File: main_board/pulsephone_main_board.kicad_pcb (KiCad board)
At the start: 6 copper layers, 49.8 x 52.8 mm, 21 parts, among them J1 Conn_2Rows-59Pins, J2 Conn_2Rows-59Pins, J4 Conn_2Rows-59Pins, J5 Conn_2Rows-59Pins, U1 TPS62840DLCR, U2 PCM5102APWR

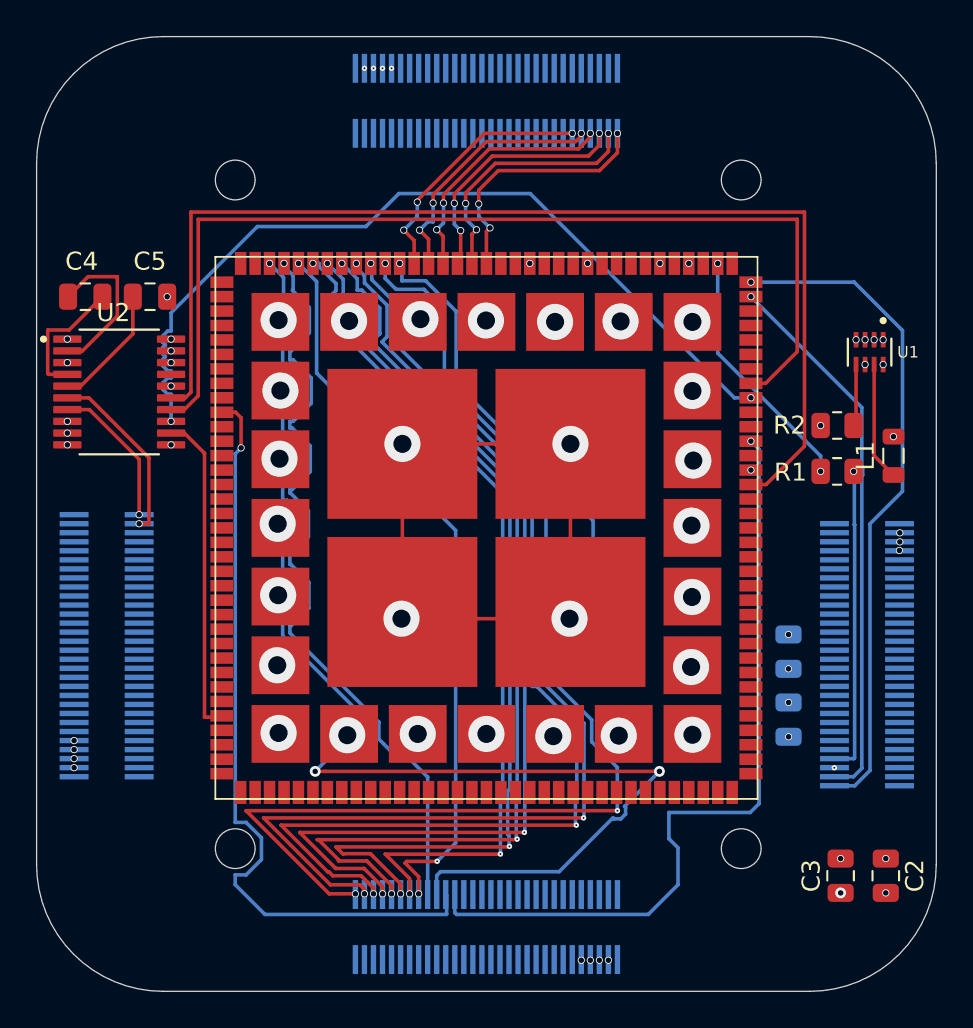
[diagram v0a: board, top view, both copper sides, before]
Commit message: replaced all power connections with copper pads and started drawing traces to them.
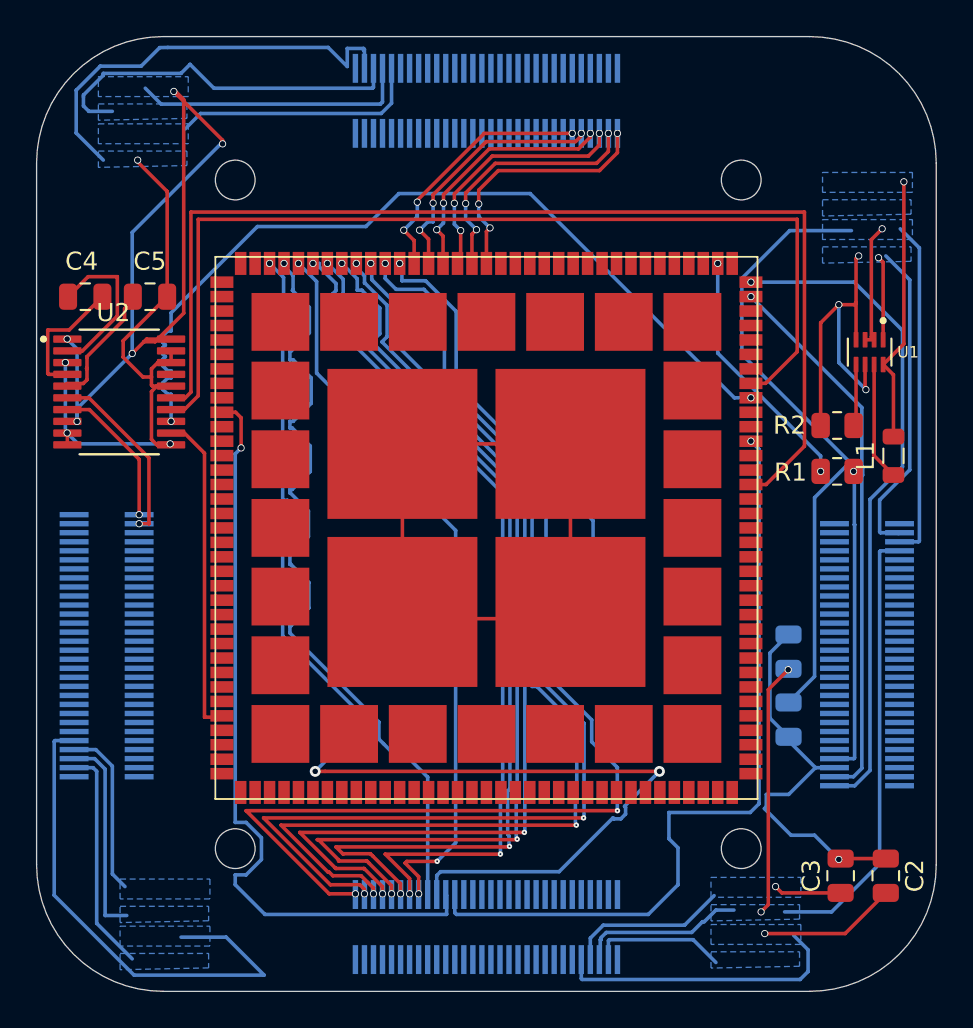
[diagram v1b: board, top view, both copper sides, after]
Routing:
- net GND: track 43.8 -> 185.7 mm, vias 50 -> 9
- net +5V: track 0.00 -> 126.6 mm, vias 12 -> 2
- net +3.3V: track 0.00 -> 97.9 mm, vias 9 -> 7
- net +3.7VBAT: track 0.00 -> 80.2 mm, vias 5 -> 2
- added copper zone on B.Cu, net +3.3V
- added copper zone on B.Cu, net +3.7VBAT
- added copper zone on B.Cu, net +5V
- added copper zone on B.Cu, net GND
- removed copper zone on In2.Cu, net +3.3V
- removed copper zone on In3.Cu, net +3.7VBAT
- removed copper zone on In1.Cu, net +5V
- removed copper zone on In4.Cu, net GND
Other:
- copper layers 6 -> 2

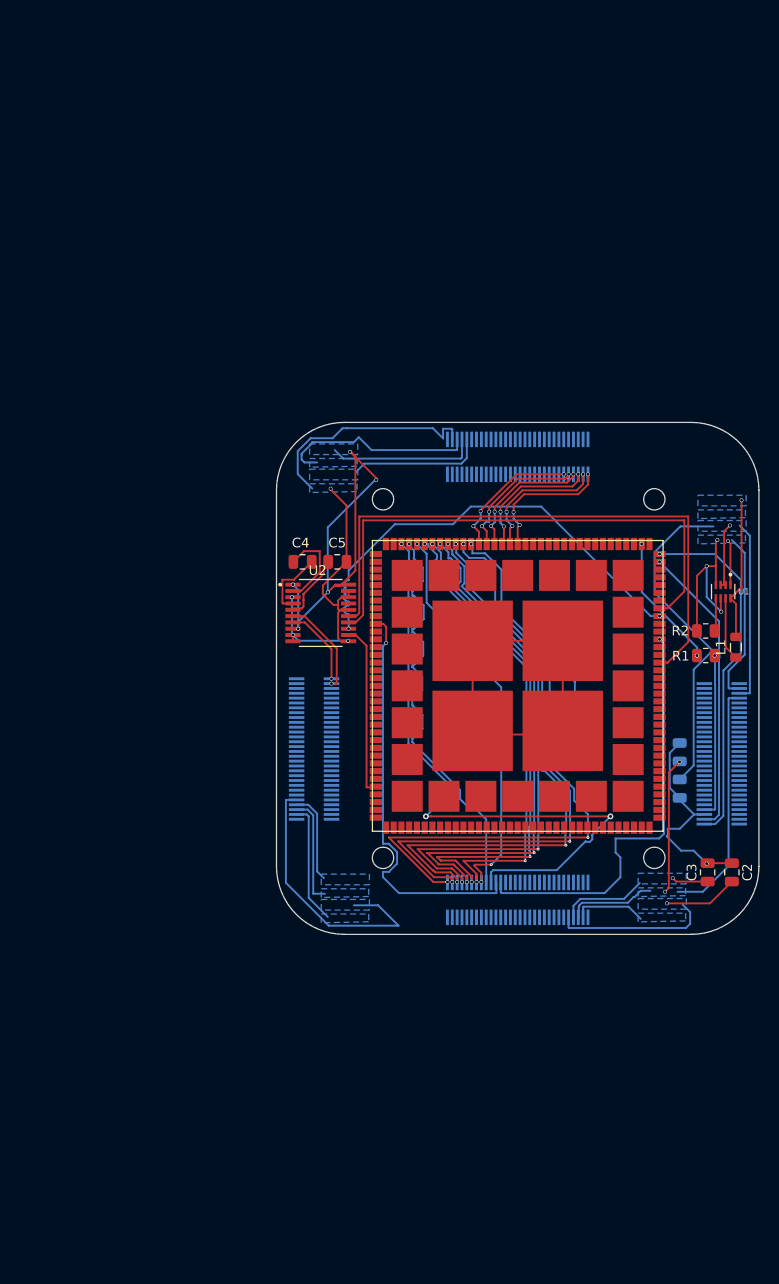
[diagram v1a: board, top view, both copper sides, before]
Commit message: Refactor the main board design
Mainboard is now one big pcb which is the shape and size of the phone. Modules will now attach on top of main board
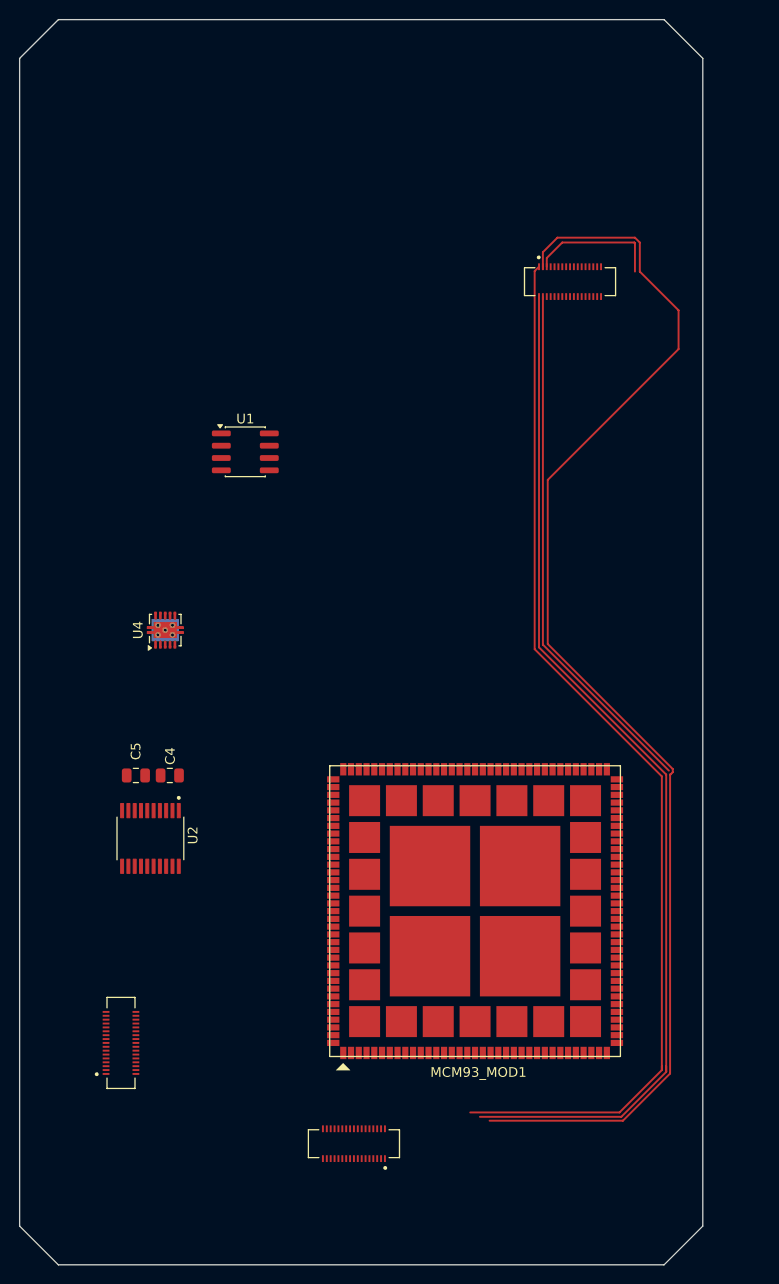
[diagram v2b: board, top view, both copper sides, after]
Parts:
- removed ? (x2): , 
- removed C1, C6: 22uF, Capacitor_SMD:C_0805_2012Metric
- removed C2: 4.7uF, Capacitor_SMD:C_0805_2012Metric
- removed C3: 10uF, Capacitor_SMD:C_0805_2012Metric
- removed G***: LOGO, LOGO
- removed J1, J2: Conn_2Rows-59Pins, Connector_Hirose:Hirose_DF12_DF12E3.0-60DP-0.5V_2x30_P0.50mm_Vertical
- removed L1: 2.2uH, Inductor_SMD:L_0805_2012Metric
- removed R1: 100Kohm, Resistor_SMD:R_0805_2012Metric
- removed R2: 267K, Resistor_SMD:R_0805_2012Metric
- removed REF** (x2): MountingHole_2.2mm_M2, MountingHole:MountingHole_2.2mm_M2
- added J3: Conn_2Rows-35Pins_MountingPin, DF40-34P:HIROSE_DF40C-34DS-0.4V_58_, F.Cu at (157.8, 53.0)
- added U4: TPS61202DRC, Package_SON:Texas_S-PVSON-N10_ThermalVias, F.Cu at (116.0, 89.0)
- J4, J5: value Conn_2Rows-59Pins -> Conn_2Rows-35Pins_MountingPin; footprint Connector_Hirose:Hirose_DF12_DF12E3.0-60DP-0.5V_2x30_P0.50mm_Vertical -> DF40-34P:HIROSE_DF40C-34DS-0.4V_58_; moved to F.Cu
- MCM93_MOD1: footprint LGA:LGA-140-080-30x30-iMX93 -> mcm-imx93_footprint:LGA-140-080-30x30-iMX93
- U1: value TPS62840DLCR -> XL1509-3.3; footprint TPS62840:SON50P200X150X100-8N -> Package_SO:SOIC-8_3.9x4.9mm_P1.27mm
- U2: footprint PCM5102APWR:SOP65P640X120-20N -> PCM5102-DAC:SOP65P640X120-20N
- moved J4 73.0 mm to (111.5, 131.6), turned to 90 degrees
- moved U1 51.4 mm to (124.3, 70.6), turned to 0 degrees
- moved J5 30.3 mm to (135.5, 142.0), turned to 180 degrees
- moved C5 30.3 mm to (113.0, 104.0), turned to 180 degrees
- moved U2 29.2 mm to (114.5, 110.5), turned to -90 degrees
- moved C4 26.0 mm to (116.5, 104.0), turned to 180 degrees
- moved MCM93_MOD1 23.7 mm to (148.0, 118.0), turned to 180 degrees
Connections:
- J4 pad 1: /CSI_CLK_N -> /DSI_CLK_N
- J4 pad 10: unconnected-(J4-Pin_10-Pad10) -> /DSI_D3_P
- J4 pad 11: unconnected-(J4-Pin_11-Pad11) -> /I2C3_SCL
- J4 pad 12: unconnected-(J4-Pin_12-Pad12) -> /I2C3_SDA
- J4 pad 13: unconnected-(J4-Pin_13-Pad13) -> +3.3V
- J4 pad 14: unconnected-(J4-Pin_14-Pad14) -> +5V
- J4 pad 15: unconnected-(J4-Pin_15-Pad15) -> +3.7VBAT
- J4 pad 16: unconnected-(J4-Pin_16-Pad16) -> GND
- J4 pad 2: /CSI_CLK_P -> /DSI_CLK_P
- J4 pad 3: /CSI_D0_N -> /DSI_D0_N
- J4 pad 4: /CSI_D0_P -> /DSI_D0_P
- J4 pad 5: /CSI_D1_N -> /DSI_D1_N
- J4 pad 6: /CSI_D1_P -> /DSI_D1_P
- J4 pad 7: unconnected-(J4-Pin_7-Pad7) -> /DSI_D2_N
- J4 pad 8: unconnected-(J4-Pin_8-Pad8) -> /DSI_D2_P
- J4 pad 9: unconnected-(J4-Pin_9-Pad9) -> /DSI_D3_N
- J5 pad 1: /DSI_CLK_N -> +3.3V
- J5 pad 10: /DSI_D3_P -> unconnected-(J5-Pin_10-Pad10)
- J5 pad 11: /I2C3_SCL -> unconnected-(J5-Pin_11-Pad11)
- J5 pad 12: /I2C3_SDA -> unconnected-(J5-Pin_12-Pad12)
- J5 pad 2: /DSI_CLK_P -> +5V
- J5 pad 3: /DSI_D0_N -> +3.7VBAT
- J5 pad 4: /DSI_D0_P -> GND
- J5 pad 5: /DSI_D1_N -> unconnected-(J5-Pin_5-Pad5)
- J5 pad 6: /DSI_D1_P -> unconnected-(J5-Pin_6-Pad6)
- J5 pad 7: /DSI_D2_N -> unconnected-(J5-Pin_7-Pad7)
- J5 pad 8: /DSI_D2_P -> unconnected-(J5-Pin_8-Pad8)
- J5 pad 9: /DSI_D3_N -> unconnected-(J5-Pin_9-Pad9)
- MCM93_MOD1 pad 11: +5V -> Net-(MCM93_MOD1-Pad11)
- MCM93_MOD1 pad 139: /USB_P -> unconnected-(MCM93_MOD1D-34-Pad139)
- MCM93_MOD1 pad 140: /USB_N -> unconnected-(MCM93_MOD1D-35-Pad140)
- MCM93_MOD1 pad 15: +5V -> Net-(MCM93_MOD1-Pad11)
- MCM93_MOD1 pad 2: Net-(MCM93_MOD1-Pad2) -> unconnected-(MCM93_MOD1-Pad2)
- MCM93_MOD1 pad 4: +5V -> Net-(MCM93_MOD1-Pad11)
- MCM93_MOD1 pad 6: +5V -> Net-(MCM93_MOD1-Pad11)
- U1 pad 1: GND -> +3.7VBAT
- U1 pad 2: +5V -> Net-(D1-K)
- U1 pad 3: +5V -> +3.3V
- U1 pad 4: GND -> unconnected-(U1-~{EN}-Pad4)
- U1 pad 5: Net-(U1-VSET) -> GND
- U1 pad 7: Net-(U1-SW) -> GND
- U1 pad 8: +3.3V -> GND
- U2 pad 6: /AUDIO_LEFT -> unconnected-(U2-OUTL-Pad6)
- U2 pad 7: /AUDIO_RIGHT -> unconnected-(U2-OUTR-Pad7)
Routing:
- net GND: track 185.7 -> 0.00 mm, vias 9 -> 0
- net +5V: track 126.6 -> 0.00 mm, vias 2 -> 0
- net /CSI_D0_N: track 13.9 -> 131.7 mm, vias 3 -> 0
- net +3.3V: track 97.9 -> 0.00 mm, vias 7 -> 0
- net /CSI_CLK_N: track 14.0 -> 110.5 mm, vias 3 -> 0
- net /CSI_CLK_P: track 14.1 -> 107.2 mm, vias 3 -> 0
- net +3.7VBAT: track 80.2 -> 0.00 mm, vias 2 -> 0
- net /DSI_D3_P: track 73.4 -> 0.00 mm, vias 3 -> 0
- net /AUDIO_DATA_OUT: track 73.3 -> 0.00 mm
- net /DSI_CLK_N: track 66.4 -> 0.00 mm, vias 3 -> 0
- net /AUDIO_FRAME_CLOCK: track 61.9 -> 0.00 mm
- net /DSI_CLK_P: track 61.4 -> 0.00 mm, vias 3 -> 0
- net /DSI_D0_N: track 59.4 -> 0.00 mm, vias 3 -> 0
- net /DSI_D0_P: track 54.3 -> 0.00 mm, vias 3 -> 0
- net /DSI_D1_N: track 53.2 -> 0.00 mm, vias 3 -> 0
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- removed copper zone on B.Cu, net +3.3V
- removed copper zone on B.Cu, net +3.7VBAT
- removed copper zone on B.Cu, net +5V
- removed copper zone on B.Cu, net GND
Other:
- board size 49.8 x 52.8 mm -> 70.5 x 128.5 mm

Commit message: Work on completing schematics and starting pcb design
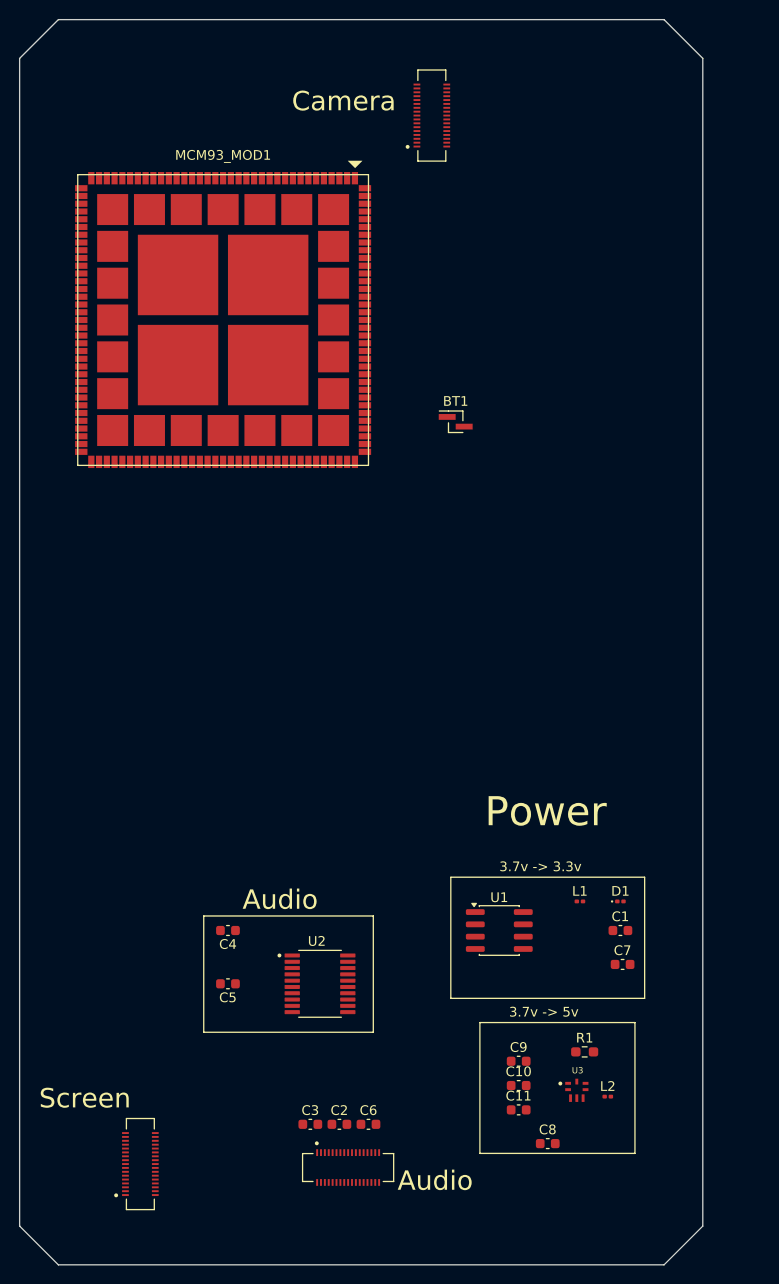
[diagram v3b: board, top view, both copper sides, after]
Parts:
- removed U4: TPS61202DRC, Package_SON:Texas_S-PVSON-N10_ThermalVias
- added BT1: Battery, Connector_PinHeader_1.00mm:PinHeader_1x02_P1.00mm_Vertical_SMD_Pin1Left, F.Cu at (146.0, 67.5)
- added C1: 20uF, Capacitor_SMD:C_0603_1608Metric, F.Cu at (163.0, 120.0)
- added C10: 22uF, Capacitor_SMD:C_0603_1608Metric, F.Cu at (152.5, 136.0)
- added C11: 22uF, Capacitor_SMD:C_0603_1608Metric, F.Cu at (152.5, 138.5)
- added C2: 10uF, Capacitor_SMD:C_0603_1608Metric, F.Cu at (134.0, 140.0)
- added C3: 10uF, Capacitor_SMD:C_0603_1608Metric, F.Cu at (131.0, 140.0)
- added C6: 10uF, Capacitor_SMD:C_0603_1608Metric, F.Cu at (137.0, 140.0)
- added C7: 20uF, Capacitor_SMD:C_0603_1608Metric, F.Cu at (163.2, 123.5)
- added C8: 22uF, Capacitor_SMD:C_0603_1608Metric, F.Cu at (155.5, 142.0)
- added C9: 22uF, Capacitor_SMD:C_0603_1608Metric, F.Cu at (152.5, 133.5)
- added D1: D_Schottky, Diode_SMD:D_0201_0603Metric, F.Cu at (163.0, 117.0)
- added L1: 47uh/2A, Inductor_SMD:L_0201_0603Metric, F.Cu at (158.8, 117.0)
- added L2: 1uH, Inductor_SMD:L_0201_0603Metric, F.Cu at (161.7, 137.1)
- added R1: 1Mega Ohm, Resistor_SMD:R_0603_1608Metric_Pad0.98x0.95mm_HandSolder, F.Cu at (159.3, 132.5)
- added U3: ~, MIC2877-5.0YFT-TR:VREG_MIC2877-AYFT-TR, F.Cu at (158.5, 136.5)
- C4, C5: footprint Capacitor_SMD:C_0805_2012Metric -> Capacitor_SMD:C_0603_1608Metric
- moved MCM93_MOD1 66.3 mm to (122.0, 57.0), turned to 0 degrees
- moved U1 55.9 mm to (150.5, 120.0)
- moved C5 23.5 mm to (122.5, 125.5)
- moved U2 23.0 mm to (132.0, 125.5), turned to 0 degrees
- moved J3 22.3 mm to (143.5, 35.9), turned to 90 degrees
- moved C4 17.1 mm to (122.5, 120.0)
- moved J4 12.7 mm to (113.5, 144.1)
- moved J5 2.53 mm to (134.9, 144.5), turned to 0 degrees
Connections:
- J5 pad 8: unconnected-(J5-Pin_8-Pad8) -> Net-(J5-Pin_8)
- J5 pad 9: unconnected-(J5-Pin_9-Pad9) -> Net-(J5-Pin_9)
- MCM93_MOD1 pad 11: Net-(MCM93_MOD1-Pad11) -> +5V
- MCM93_MOD1 pad 133: /AUDIO_DATA_OUT -> /SAI_MASTERCLOCK
- MCM93_MOD1 pad 15: Net-(MCM93_MOD1-Pad11) -> +5V
- MCM93_MOD1 pad 4: Net-(MCM93_MOD1-Pad11) -> +5V
- MCM93_MOD1 pad 6: Net-(MCM93_MOD1-Pad11) -> +5V
- U1 pad 4: unconnected-(U1-~{EN}-Pad4) -> +3.7VBAT
- U2 pad 12: /AUDIO_DATA_OUT -> /SAI_MASTERCLOCK
- U2 pad 6: unconnected-(U2-OUTL-Pad6) -> Net-(J5-Pin_8)
- U2 pad 7: unconnected-(U2-OUTR-Pad7) -> Net-(J5-Pin_9)
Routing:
- net /CSI_D0_N: track 131.7 -> 0.00 mm
- net /CSI_CLK_N: track 110.5 -> 0.00 mm
- net /CSI_CLK_P: track 107.2 -> 0.00 mm
- net /CSI_D0_P: track 54.3 -> 0.00 mm
- net /CSI_D1_N: track 13.6 -> 0.00 mm
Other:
- board text added: "3.7v -> 3.3v"
- board text added: "3.7v -> 5v"
- board text added: "Audio"
- board text added: "Camera"
- board text added: "Power"
- board text added: "Screen"

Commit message: Add charging IC and USB-C to schematic and PCB
Next step is to review PCB layout and start drawing traces
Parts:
- added C12: 10uF, Capacitor_SMD:C_0603_1608Metric, F.Cu at (127.7, 145.0)
- added C13: 10uF, Capacitor_SMD:C_0603_1608Metric, F.Cu at (127.7, 147.5)
- added J1: USB_C_Receptacle_USB2.0_14P, Connector_USB:USB_C_Receptacle_Amphenol_12401548E4-2A, F.Cu at (138.4, 150.1)
- added U5: TP4056-42-ESOP8, Package_SO:SOIC-8-1EP_3.9x4.9mm_P1.27mm_EP2.41x3.3mm_ThermalVias, F.Cu at (121.5, 147.1)
- moved J5 18.2 mm to (153.0, 146.5)
- moved C4 6.26 mm to (127.9, 116.8)
- moved C5 6.26 mm to (127.9, 122.3)
- moved U2 6.26 mm to (137.4, 122.3)
